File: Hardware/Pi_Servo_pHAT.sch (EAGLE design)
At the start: 110 parts, among them J1 RASPBERRYPI-40-PIN-GPIO, J19 QWIIC, J20 USB C, J21 RVR, Q1 310mA/60V/1.6Ω, Q12 20V/4.2A/52mΩ/1.4W, Q2 20V/4.2A/52mΩ/1.4W, Q4 310mA/60V/1.6Ω, Q5 20V/4.2A/52mΩ/1.4W, Q7 20V/4.2A/52mΩ/1.4W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

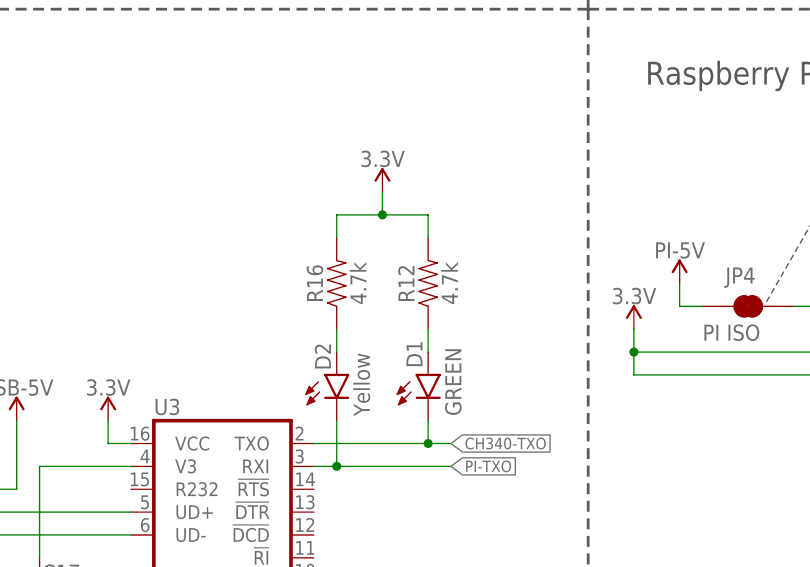
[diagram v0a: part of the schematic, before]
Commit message: Updating resistor values for LEDs
330 for green and 1K for yellow.
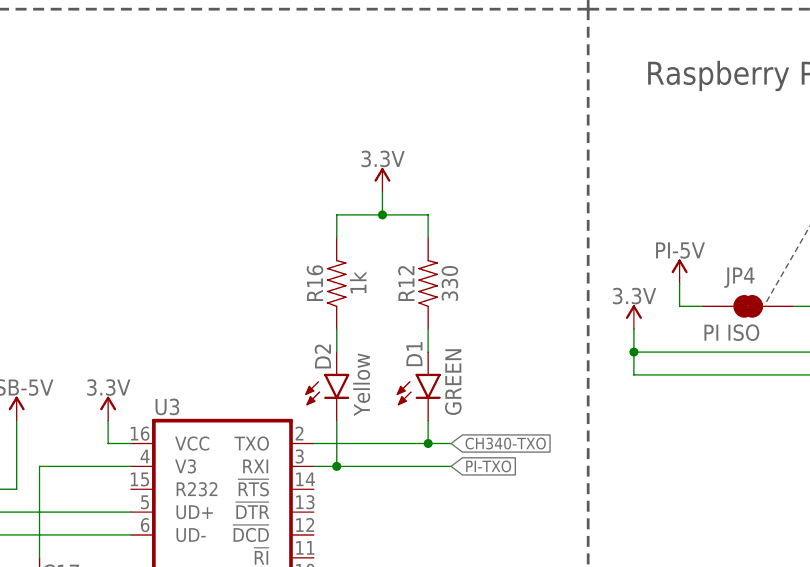
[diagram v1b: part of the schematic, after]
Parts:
- R12: value 4.7k -> 330; device SparkFun-Resistors:4.7KOHM-0603-1/10W-1% -> SparkFun-Resistors:330OHM-0603-1/10W-1%
- R16: value 4.7k -> 1k; device SparkFun-Resistors:4.7KOHM-0603-1/10W-1% -> SparkFun-Resistors:1KOHM-0603-1/10W-1%
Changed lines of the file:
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@@
 <?xml version="1.0" encoding="utf-8"?>
 <!DOCTYPE eagle SYSTEM "eagle.dtd">
-<eagle version="9.4.0">
+<eagle version="9.4.2">
 <drawing>
 <settings>
@@
 <part name="C17" library="SparkFun-Capacitors" deviceset="10NF" device="-0603-50V-10%" value="10nF"/>
 <part name="GND32" library="SparkFun-PowerSymbols" deviceset="GND" device=""/>
-<part name="R12" library="SparkFun-Resistors" deviceset="4.7KOHM" device="-0603-1/10W-1%" value="4.7k"/>
-<part name="R16" library="SparkFun-Resistors" deviceset="4.7KOHM" device="-0603-1/10W-1%" value="4.7k"/>
+<part name="R12" library="SparkFun-Resistors" deviceset="330OHM" device="-0603-1/10W-1%" value="330"/>
+<part name="R16" library="SparkFun-Resistors" deviceset="1KOHM" device="-0603-1/10W-1%" value="1k"/>
 <part name="J20" library="SparkFun-Connectors" deviceset="USB_C" device="16PIN" value="USB C"/>
 <part name="GND38" library="SparkFun-PowerSymbols" deviceset="GND" device=""/>
